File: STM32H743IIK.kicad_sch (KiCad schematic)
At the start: 31 parts, among them U1 STM32H743IIKx, Y1 25MHz, Y2 32.768KHz

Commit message: Add power
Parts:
- added C38: 1u, Capacitor_SMD:C_0402_1005Metric, symbol Device:C
- added C39: 100n, Capacitor_SMD:C_0201_0603Metric, symbol Device:C_Small
- added L1: L_Small, Inductor_SMD:L_0402_1005Metric, symbol Device:L_Small
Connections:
- net FLASH_CLK: now also U1.M6 (PB2)
- net FLASH_DI(IO0): now also U1.L3 (PF8)
- net FLASH_DO(IO1): now also U1.L2 (PF9)
- net FLASH_IO2: now also U1.K1 (PF7)
- net FLASH_IO3: now also U1.K2 (PF6)
- net GND: now also C38.2, C39.1
- net SDRAM_BA0: now also U1.K14 (PG4)
- net SDRAM_BA1: now also U1.K13 (PG5)
- net SDRAM_CKE: now also U1.F4 (PH2)
- net SDRAM_CLK: now also U1.H14 (PG8)
- net SDRAM_DQMH: now also U1.A3 (PE1)
- net SDRAM_DQML: now also U1.A4 (PE0)
- net ~{FLASH_CS}: now also U1.B6 (PB6)
- net ~{SDRAM_CAS}: now also U1.B7 (PG15)
- net ~{SDRAM_CS}: now also U1.M4 (PC2_C)
- net ~{SDRAM_RAS}: now also U1.R6 (PF11)
- net ~{SDRAM_WE}: now also U1.J4 (PH5)
- net USB_DP: now reaches U1.B15 (PA12)
- net USB_DN: now reaches U1.C15 (PA11)
- net USB_VBUS_DET: now reaches U1.E15 (PA9)
- net SDRAM_A0: now reaches U1.E2 (PF0)
- net SDRAM_A2: now reaches U1.H2 (PF2)
- net SDRAM_A1: now reaches U1.H3 (PF1)
- net SDRAM_A3: now reaches U1.J2 (PF3)
- net SDRAM_A4: now reaches U1.J3 (PF4)
- net SDRAM_A5: now reaches U1.K3 (PF5)
- net SDRAM_A12: now reaches U1.L15 (PG2)
- net SDRAM_A11: now reaches U1.M7 (PG1)
- net SDRAM_A7: now reaches U1.N6 (PF13)
- net SDRAM_A10: now reaches U1.N7 (PG0)
- net SDRAM_A6: now reaches U1.P6 (PF12)
- net SDRAM_A9: now reaches U1.P7 (PF15)
- net SDRAM_A8: now reaches U1.R7 (PF14)
- net +3V3 renamed VDD_MCU
- net VDD_MCU: now also L1.1; no longer C8.1, C9.2, U1.P1 (VREF+), U1.R1 (VDDA)
- new net VDDA: C38.1, C39.2, C8.1, C9.2, L1.2, U1.P1 (VREF+), U1.R1 (VDDA)
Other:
- moved on the sheet: C4, C5, Y1

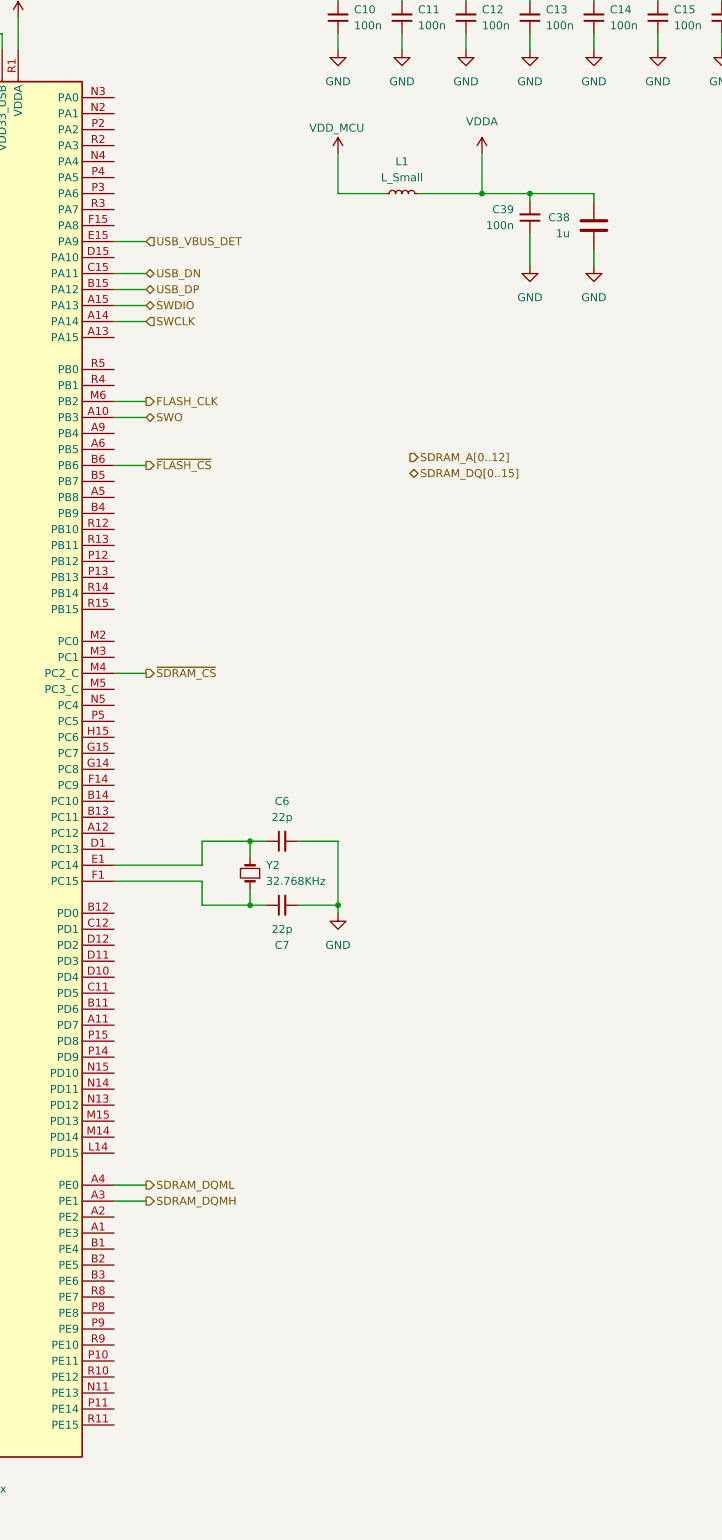
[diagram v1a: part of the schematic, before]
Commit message: Change to 8 layer, doing SDRAM traces
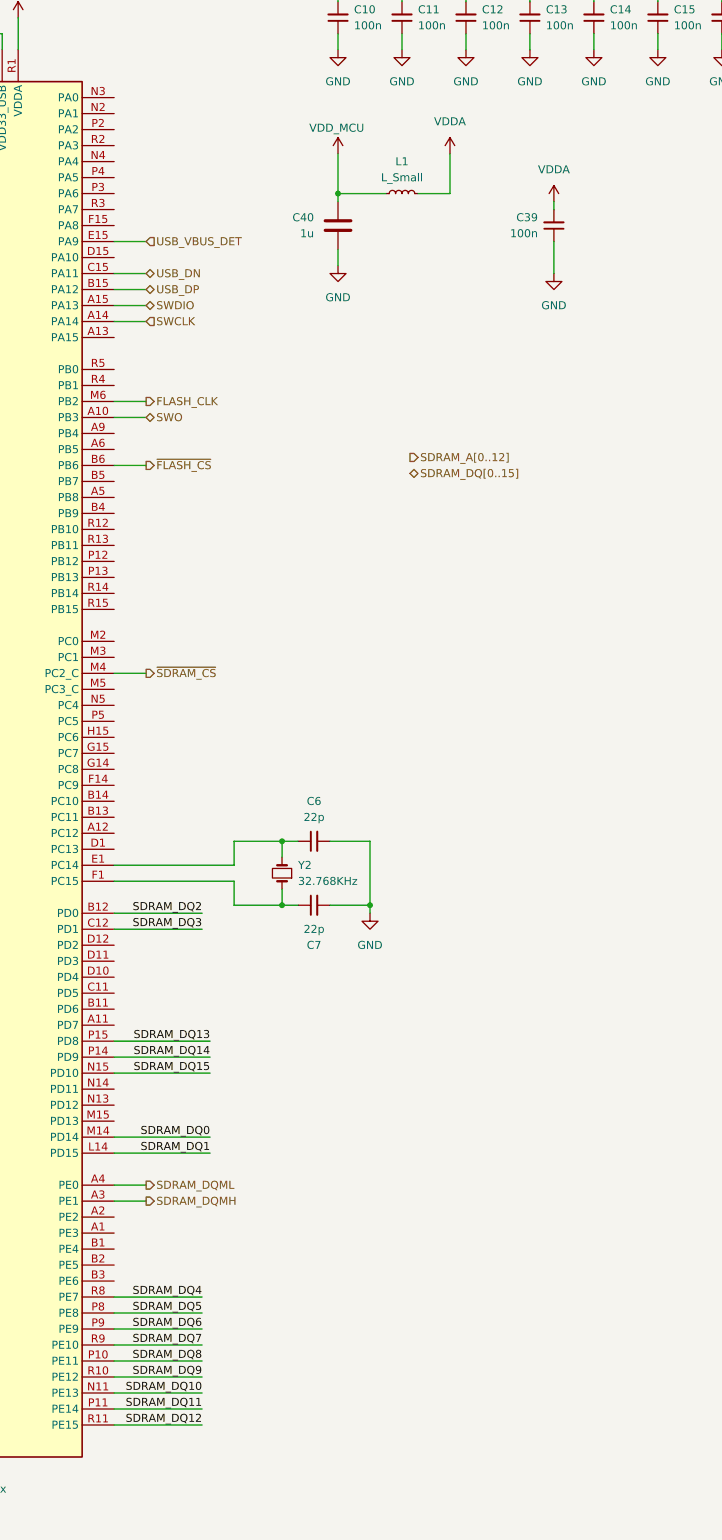
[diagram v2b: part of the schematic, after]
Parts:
- removed C38: 1u, Capacitor_SMD:C_0402_1005Metric, symbol Device:C
- added C40: 1u, Capacitor_SMD:C_0402_1005Metric, symbol Device:C
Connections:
- net GND: now also C40.2
- net VDD_MCU: now also C40.1
- net SDRAM_DQ2: now reaches U1.B12 (PD0)
- net SDRAM_DQ3: now reaches U1.C12 (PD1)
- net SDRAM_DQ1: now reaches U1.L14 (PD15)
- net SDRAM_DQ0: now reaches U1.M14 (PD14)
- net SDRAM_DQ10: now reaches U1.N11 (PE13)
- net SDRAM_DQ15: now reaches U1.N15 (PD10)
- net SDRAM_DQ8: now reaches U1.P10 (PE11)
- net SDRAM_DQ11: now reaches U1.P11 (PE14)
- net SDRAM_DQ14: now reaches U1.P14 (PD9)
- net SDRAM_DQ13: now reaches U1.P15 (PD8)
- net SDRAM_DQ5: now reaches U1.P8 (PE8)
- net SDRAM_DQ6: now reaches U1.P9 (PE9)
- net SDRAM_DQ9: now reaches U1.R10 (PE12)
- net SDRAM_DQ12: now reaches U1.R11 (PE15)
- net SDRAM_DQ4: now reaches U1.R8 (PE7)
- net SDRAM_DQ7: now reaches U1.R9 (PE10)
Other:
- moved on the sheet: C39, C6, C7, Y2

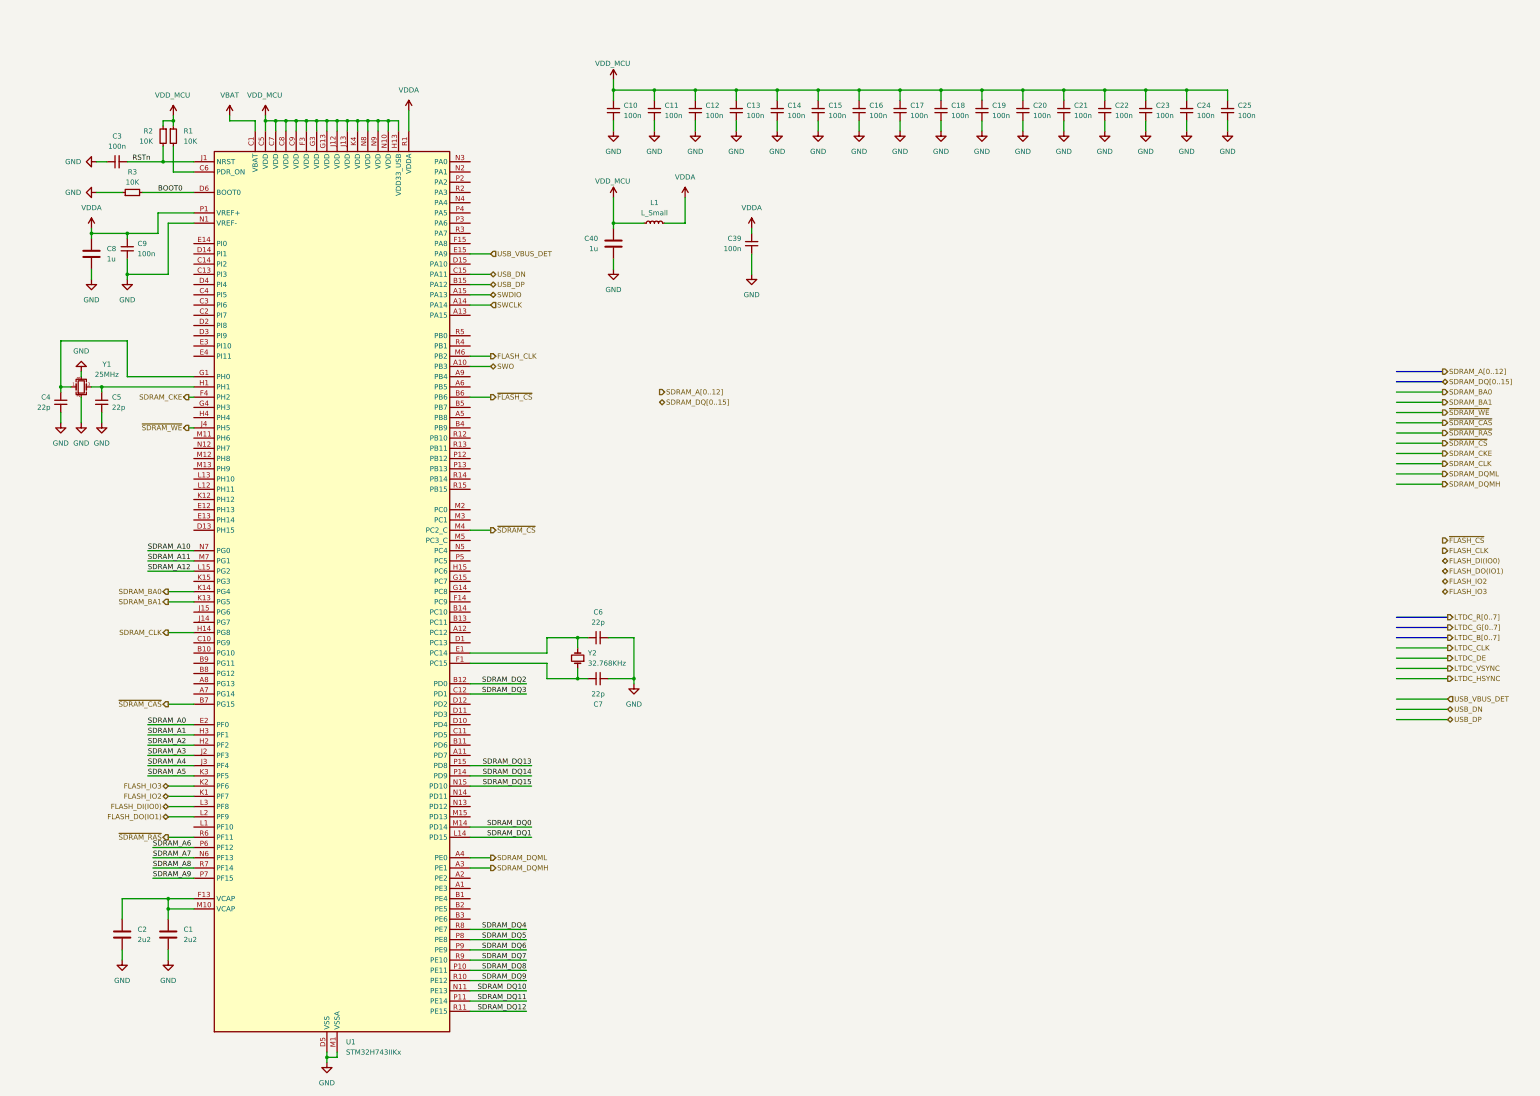
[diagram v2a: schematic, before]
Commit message: Finished SDRAM, QSPI FLASH (trace length not matched yet)
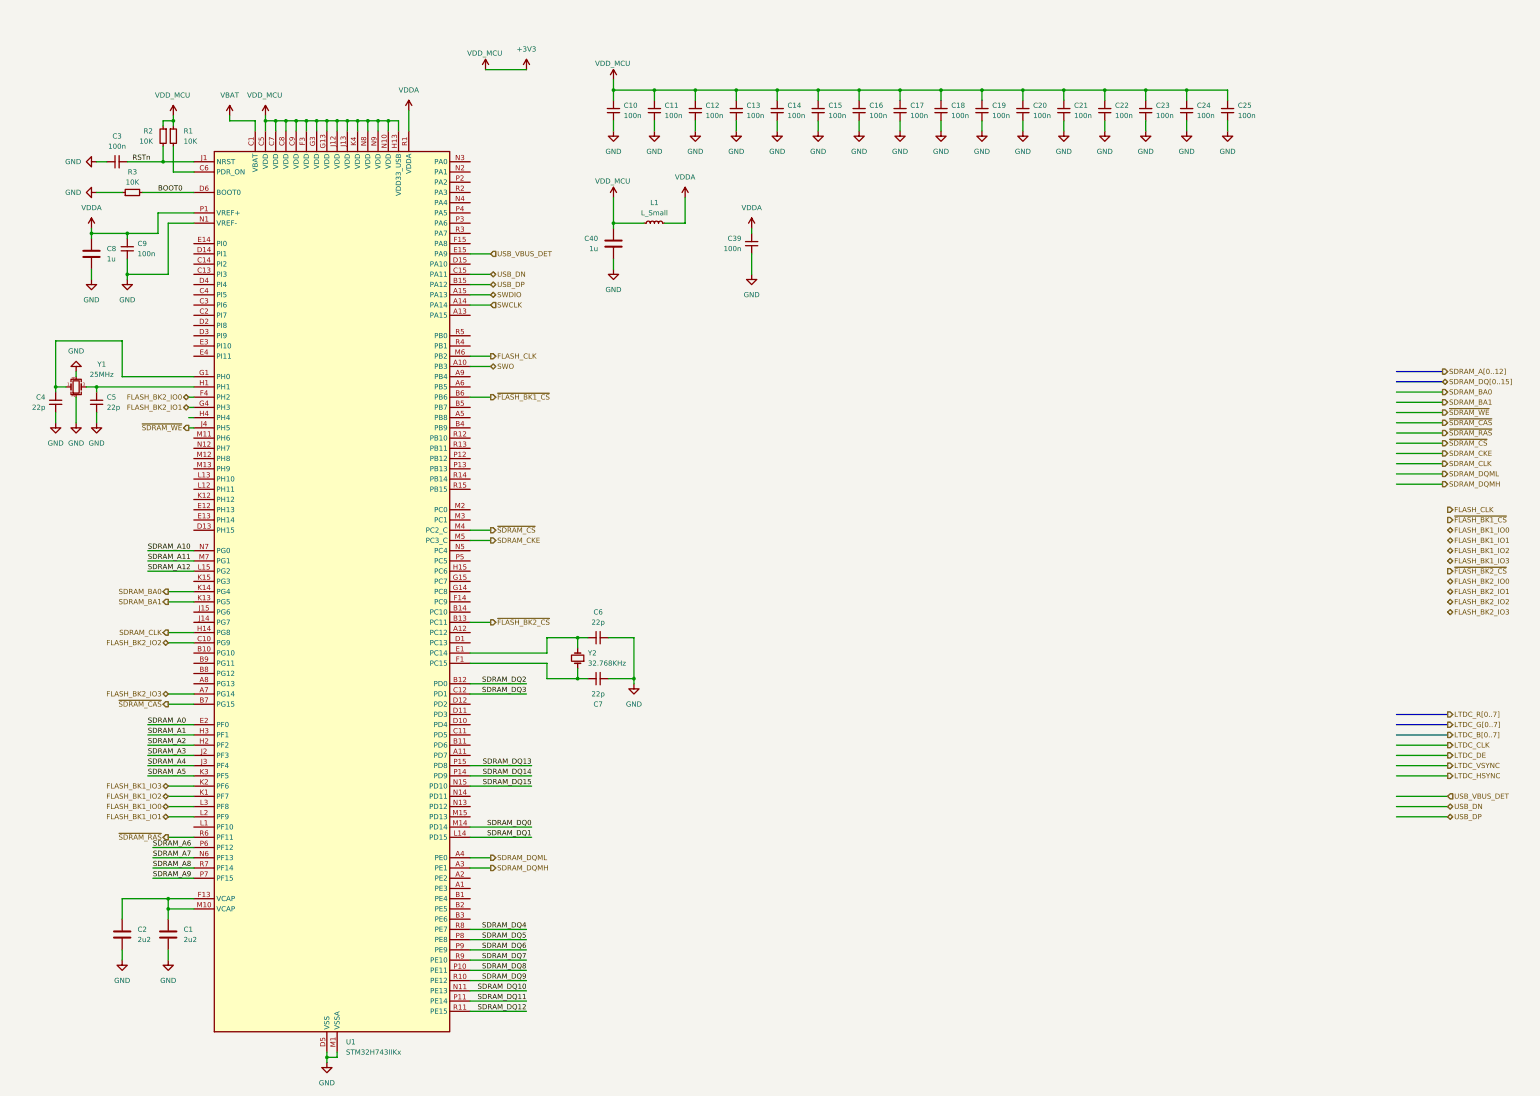
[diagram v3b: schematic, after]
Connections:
- net SDRAM_CKE: now also U1.M5 (PC3_C); no longer U1.F4 (PH2)
- net FLASH_BK2_IO3: now reaches U1.A7 (PG14)
- net ~{FLASH_BK2_CS}: now reaches U1.B13 (PC11)
- net FLASH_BK2_IO2: now reaches U1.C10 (PG9)
- net FLASH_BK2_IO1: now reaches U1.G4 (PH3)
- net FLASH_DI(IO0) renamed FLASH_BK1_IO0
- net FLASH_DO(IO1) renamed FLASH_BK1_IO1
- net FLASH_IO2 renamed FLASH_BK1_IO2
- net FLASH_IO3 renamed FLASH_BK1_IO3
- net VDD_MCU renamed +3V3
- net ~{FLASH_CS} renamed ~{FLASH_BK1_CS}
- new net FLASH_BK2_IO0: U1.F4 (PH2)
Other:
- moved on the sheet: C4, C5, Y1

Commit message: Finished LTDC tracks
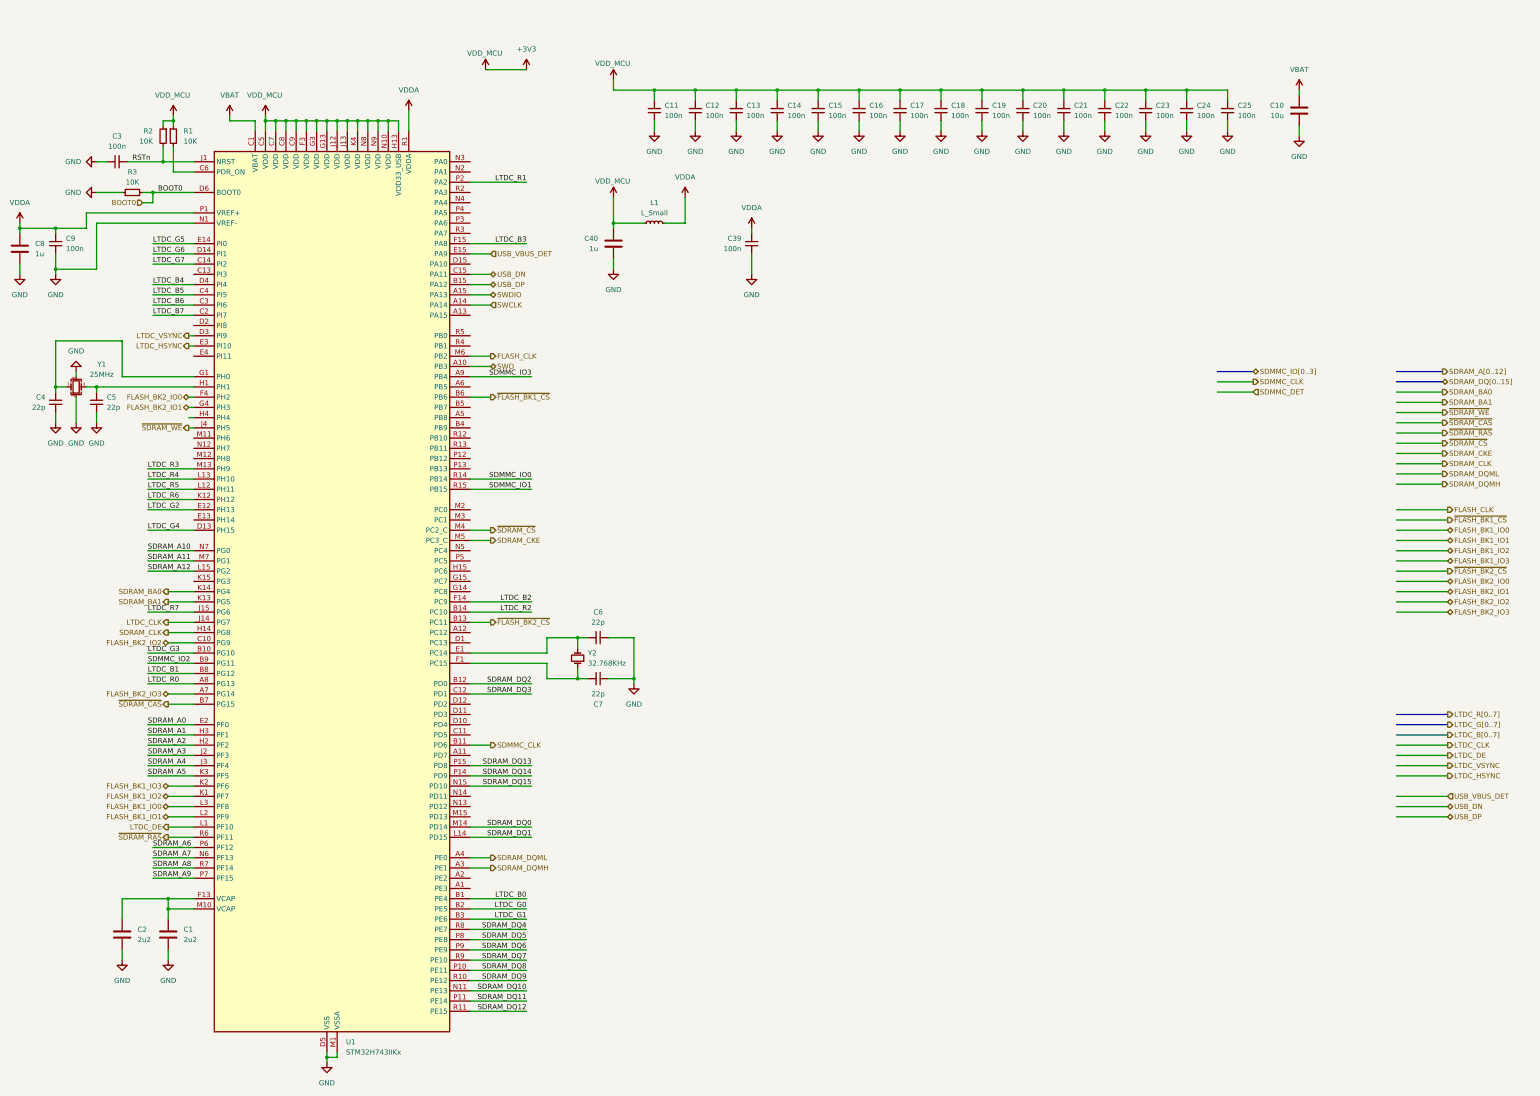
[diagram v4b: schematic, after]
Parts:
- removed C10: 100n, Capacitor_SMD:C_0201_0603Metric, symbol Device:C_Small
- added C10: 10u, Capacitor_SMD:C_0402_1005Metric, symbol Device:C
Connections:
- net GND: now also C10.2
- net LTDC_CLK: now also U1.J14 (PG7)
- net LTDC_DE: now also U1.L1 (PF10)
- net LTDC_HSYNC: now also U1.E3 (PI10)
- net LTDC_VSYNC: now also U1.D3 (PI9)
- net VBAT: now also C10.1
- net LTDC_R0: now reaches U1.A8 (PG13)
- net SDMMC_IO3: now reaches U1.A9 (PB4)
- net LTDC_B0: now reaches U1.B1 (PE4)
- net LTDC_G3: now reaches U1.B10 (PG10)
- net SDMMC_CLK: now reaches U1.B11 (PD6)
- net LTDC_R2: now reaches U1.B14 (PC10)
- net LTDC_G0: now reaches U1.B2 (PE5)
- net LTDC_G1: now reaches U1.B3 (PE6)
- net LTDC_B1: now reaches U1.B8 (PG12)
- net SDMMC_IO2: now reaches U1.B9 (PG11)
- net LTDC_G7: now reaches U1.C14 (PI2)
- net LTDC_B7: now reaches U1.C2 (PI7)
- net LTDC_B6: now reaches U1.C3 (PI6)
- net LTDC_B5: now reaches U1.C4 (PI5)
- net LTDC_G4: now reaches U1.D13 (PH15)
- net LTDC_G6: now reaches U1.D14 (PI1)
- net LTDC_B4: now reaches U1.D4 (PI4)
- net LTDC_G2: now reaches U1.E12 (PH13)
- net LTDC_G5: now reaches U1.E14 (PI0)
- net LTDC_B2: now reaches U1.F14 (PC9)
- net LTDC_B3: now reaches U1.F15 (PA8)
- net LTDC_R7: now reaches U1.J15 (PG6)
- net LTDC_R6: now reaches U1.K12 (PH12)
- net LTDC_R5: now reaches U1.L12 (PH11)
- net LTDC_R4: now reaches U1.L13 (PH10)
- net LTDC_R3: now reaches U1.M13 (PH9)
- net LTDC_R1: now reaches U1.P2 (PA2)
- net SDMMC_IO0: now reaches U1.R14 (PB14)
- net SDMMC_IO1: now reaches U1.R15 (PB15)
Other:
- moved on the sheet: C8, C9

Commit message: test remote connection
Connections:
- net SDMMC_CMD: now reaches U1.A11 (PD7)
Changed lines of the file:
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@@
 	(wire
 		(pts
+			(xy 313.69 109.22) (xy 322.58 109.22)
+		)
+		(stroke
+			(width 0)
+			(type default)
+		)
+	)
+	(wire
+		(pts
 			(xy 48.26 128.27) (xy 59.69 128.27)
 		)
@@
 	(wire
 		(pts
-			(xy 313.69 109.22) (xy 322.58 109.22)
+			(xy 313.69 111.76) (xy 322.58 111.76)
 		)
 		(stroke
@@
 	(wire
 		(pts
+			(xy 133.35 199.39) (xy 128.27 199.39)
+		)
+		(stroke
+			(width 0)
+			(type default)
+		)
+	)
+	(wire
+		(pts
 			(xy 128.27 207.01) (xy 143.51 207.01)
 		)
@@
 	(hierarchical_label "SDMMC_DET"
 		(shape input)
-		(at 322.58 109.22 0)
+		(at 322.58 111.76 0)
 		(fields_autoplaced yes)
 		(effects
@@
 		)
 	)
+	(hierarchical_label "SDMMC_CMD"
+		(shape output)
+		(at 133.35 199.39 0)
+		(fields_autoplaced yes)
+		(effects
+			(font
+				(size 1.27 1.27)
+			)
+			(justify left)
+		)
+	)
 	(hierarchical_label "FLASH_BK2_IO1"
 		(shape bidirectional)
@@
 		(fields_autoplaced yes)
 		(effects
+			(font
+				(size 1.27 1.27)
+			)
+			(justify left)
+		)
+	)
+	(hierarchical_label "SDMMC_CMD"
+		(shape output)
+		(at 322.58 109.22 0)
+		(fields_autoplaced yes)
+		(effects
